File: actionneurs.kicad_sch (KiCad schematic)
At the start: 93 parts, among them J1 690367280876, J10 ESC_35_1_P, J11 690367280876, J12 ESC_35_2_S, J13 Alim Pompe, J14 690367280876, J16 690367280876, J17 690367280876, J18 690367280876, J19 Alim EV, J20 Alim EV, J21 Alim EV, J22 Alim EV, J23 Alim EV, J24 Alim EV, J25 Alim EV, J26 Alim EV, J27 Alim EV, J28 Alim EV, J29 Alim EV, J30 Alim EV, J6 ESC_35_1_P, J9 ESC_35_1_S, Q1 G2302, Q10 G2302, Q11 G2302, Q12 G2302, Q13 G2302, Q14 G2302, Q15 G2302, Q16 G2302, Q17 G2302, Q18 G2302, Q2 G2302, Q3 G2302, Q4 G2302, Q5 G2302

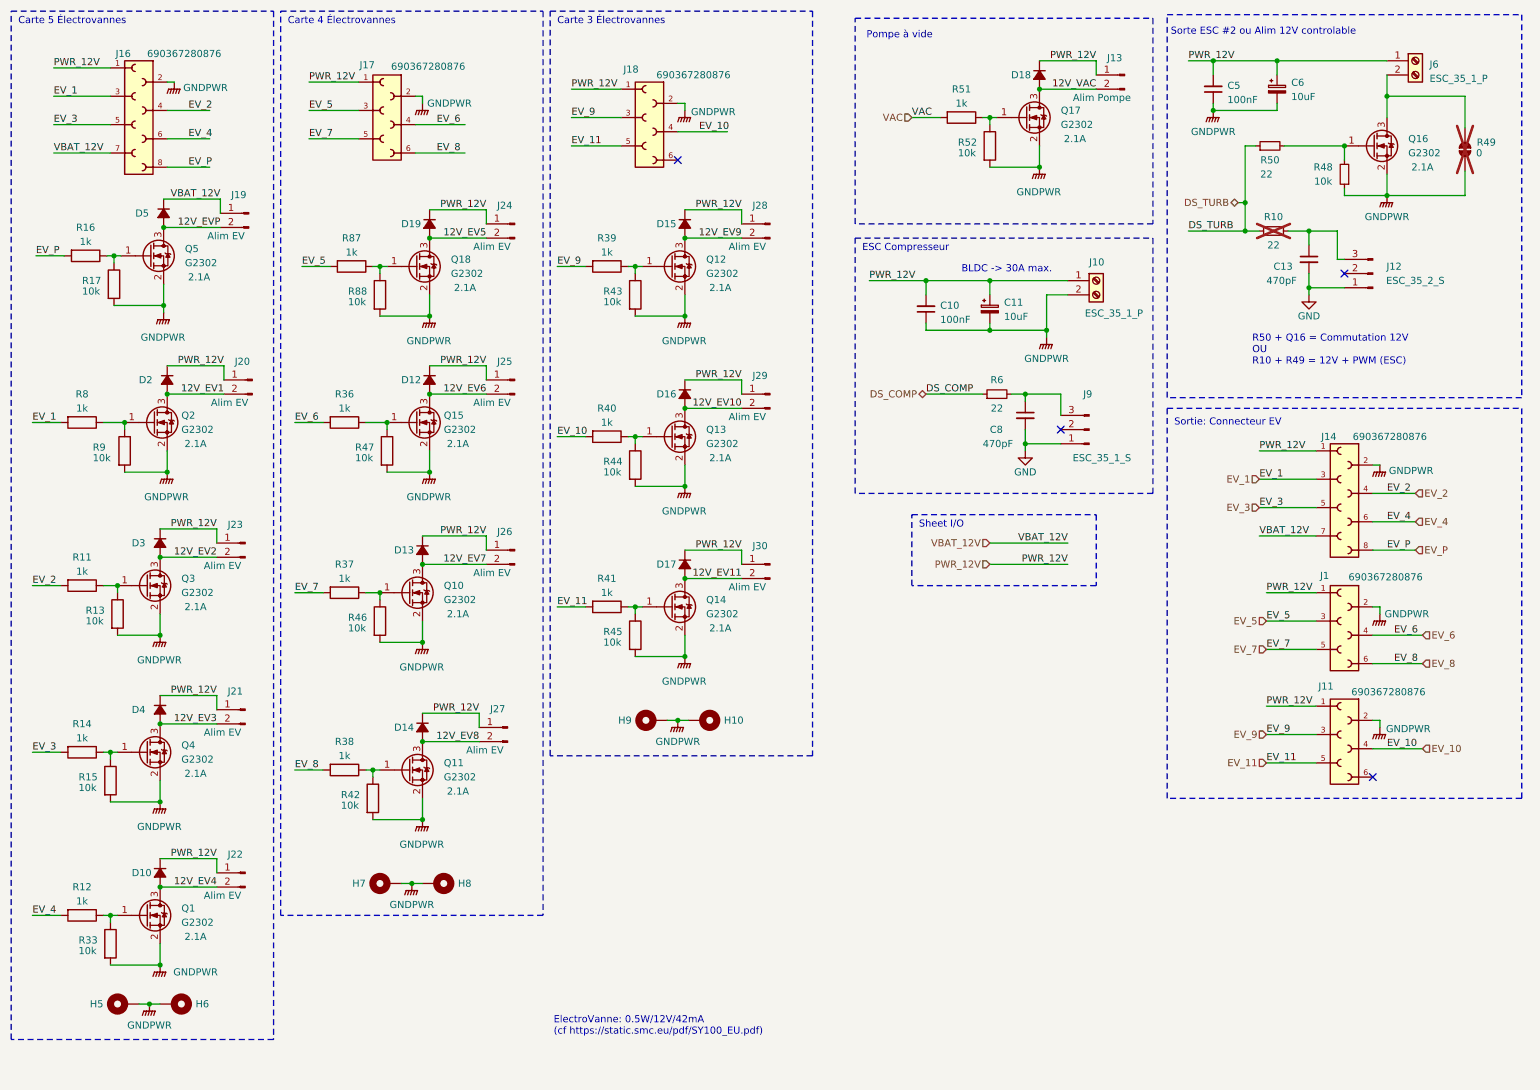
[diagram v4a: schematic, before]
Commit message: ajout regle routage JLCPCB, fin placement grossier et debut reassignation. ajout de led temoin, homogeinisation empreinte passif et remplacement 0ohm par empreintre jumper PCB 0402.
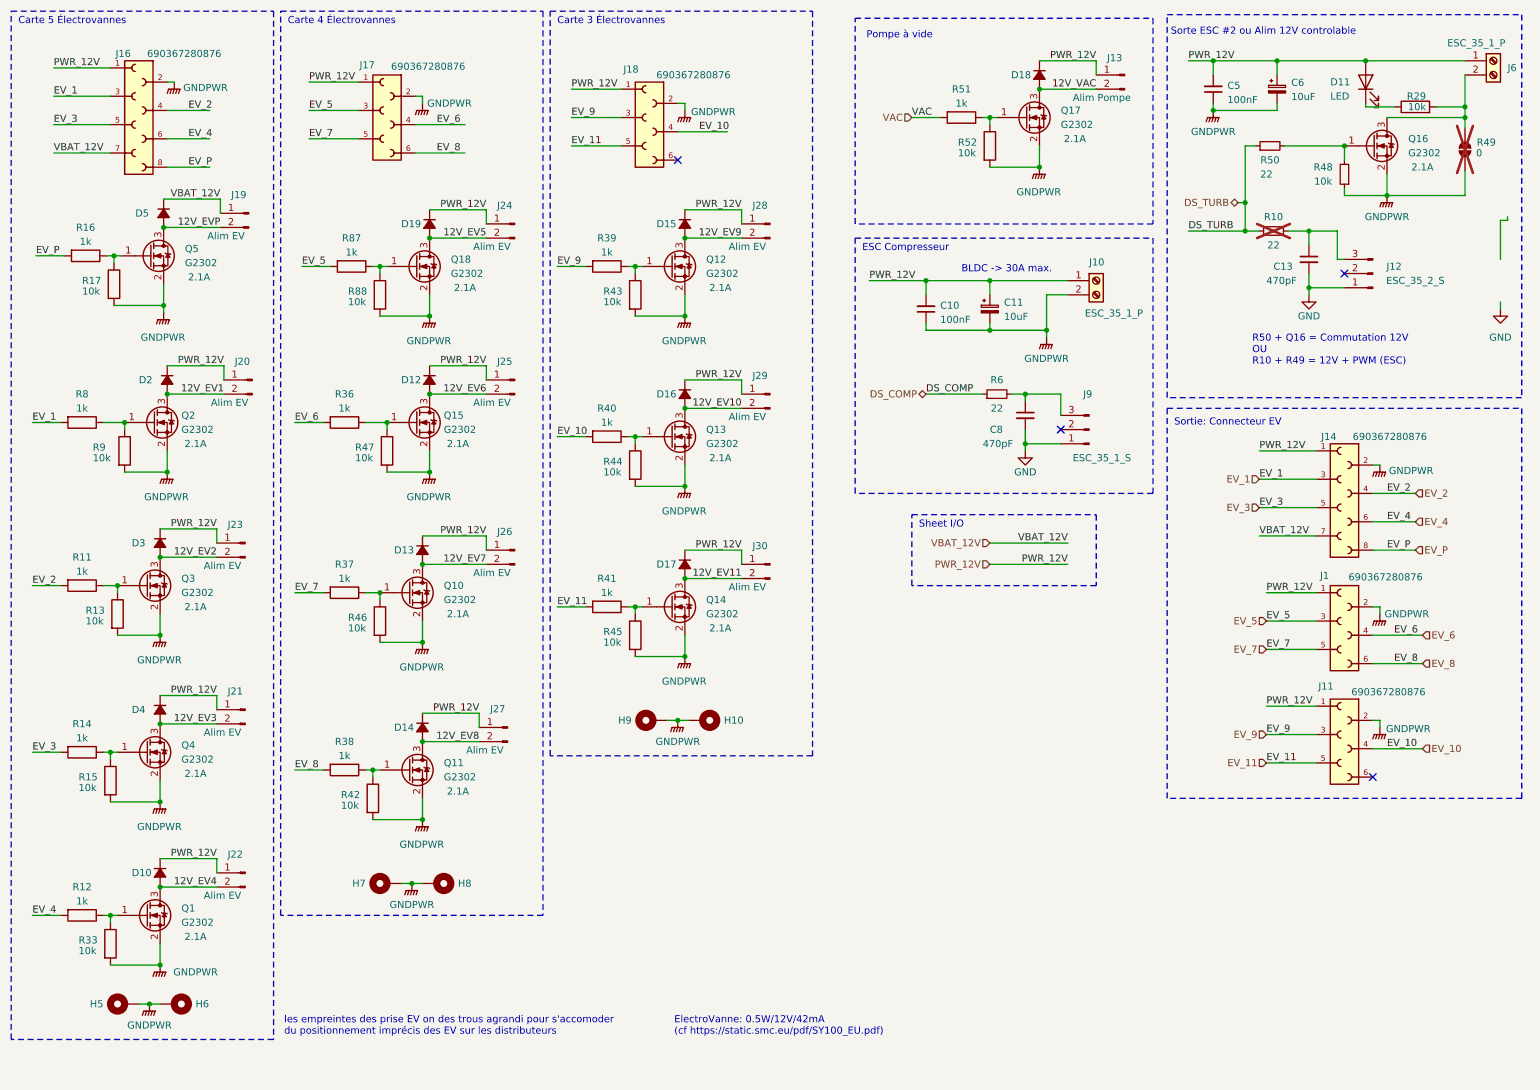
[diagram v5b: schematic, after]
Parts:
- added D11: LED, LED_SMD:LED_0603_1608Metric, symbol Device:LED
- added R29: 10k, Resistor_SMD:R_0603_1608Metric, symbol Device:R
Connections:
- net PWR_12V: now also D11.2 (A)
- net at J6.2 (Pin_2), Q16.3 (D), R49.1 (A): now also R29.2
- new net: D11.1 (K), R29.1
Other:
- note added: "les empreintes des prise EV on des trous agrandi pour s'accomoder du positionnement imprécis des EV sur les distributeurs"
- moved on the sheet: J6

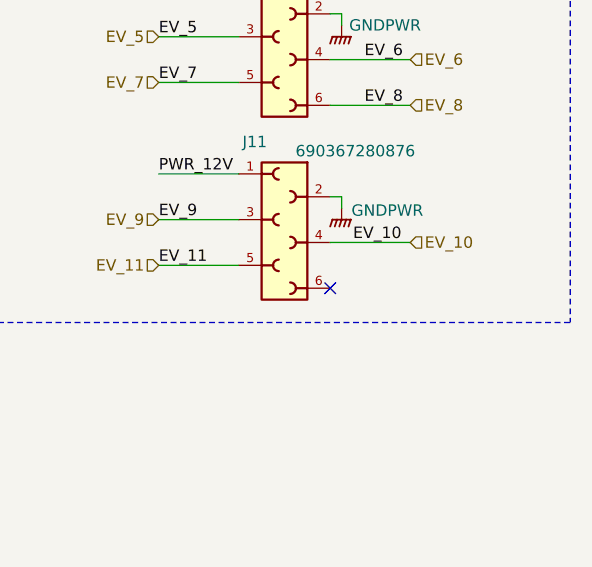
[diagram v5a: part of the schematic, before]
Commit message: fin du placement et reassignation des pins uC
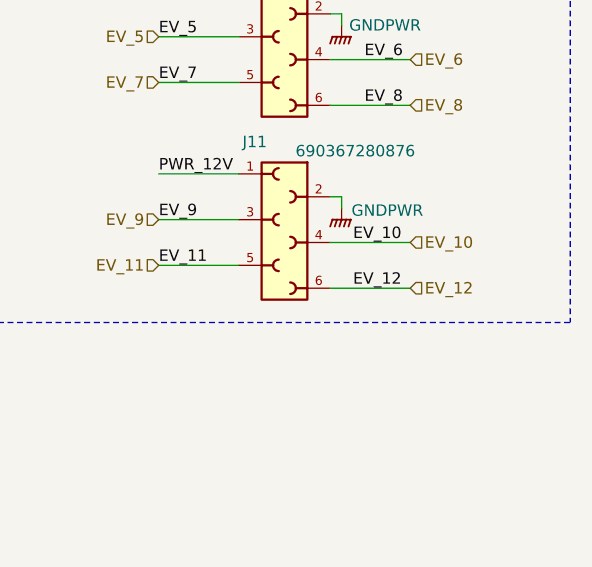
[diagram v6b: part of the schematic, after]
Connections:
- net EV_12: now reaches J11.6
- no-connect marks 4 -> 3
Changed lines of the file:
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@@
 	)
 	(no_connect
-		(at 256.54 149.86)
-	)
-	(no_connect
 		(at 132.08 39.37)
 	)
@@
 	(wire
 		(pts
+			(xy 256.54 149.86) (xy 265.43 149.86)
+		)
+		(stroke
+			(width 0)
+			(type default)
+		)
+	)
+	(wire
+		(pts
 			(xy 41.91 25.4) (xy 40.64 25.4)
 		)
@@
 		)
 	)
+	(label "EV_12"
+		(at 259.08 149.86 0)
+		(effects
+			(font
+				(size 1.27 1.27)
+			)
+			(justify left bottom)
+		)
+	)
 	(label "EV_1"
 		(at 236.22 96.52 0)
@@
 		)
 	)
+	(hierarchical_label "EV_12"
+		(shape input)
+		(at 265.43 149.86 0)
+		(effects
+			(font
+				(size 1.27 1.27)
+			)
+			(justify left)
+		)
+	)

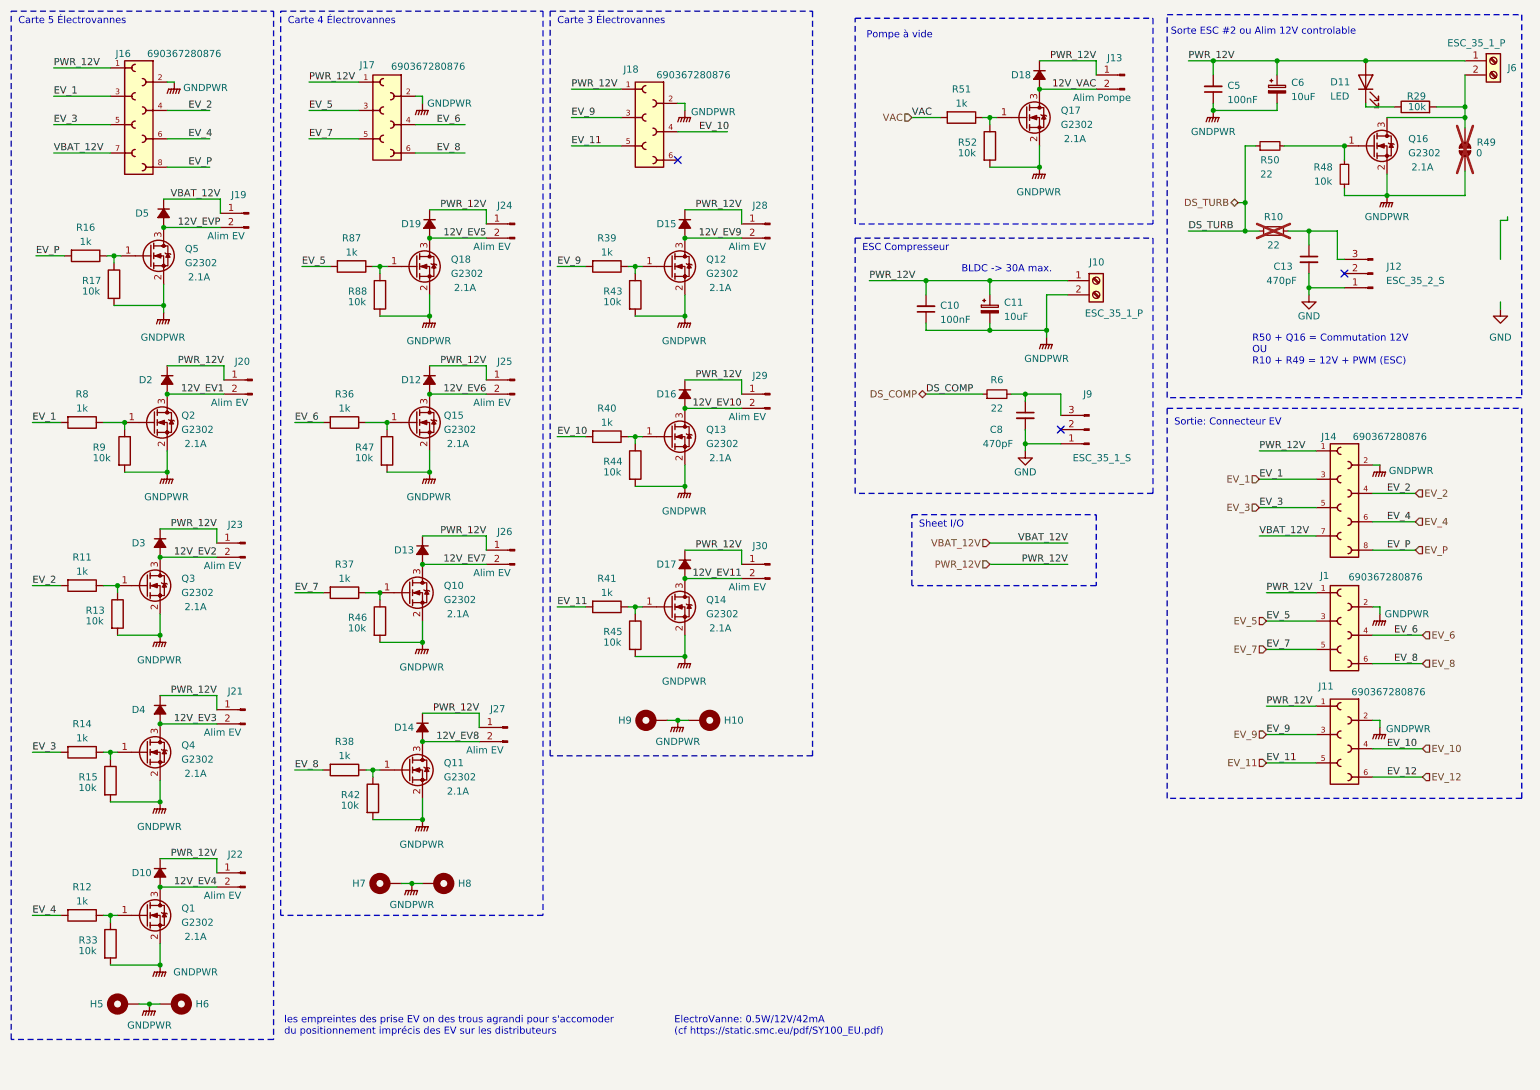
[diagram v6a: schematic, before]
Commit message: nettoyage dossier et assignation de ref JLCPCB
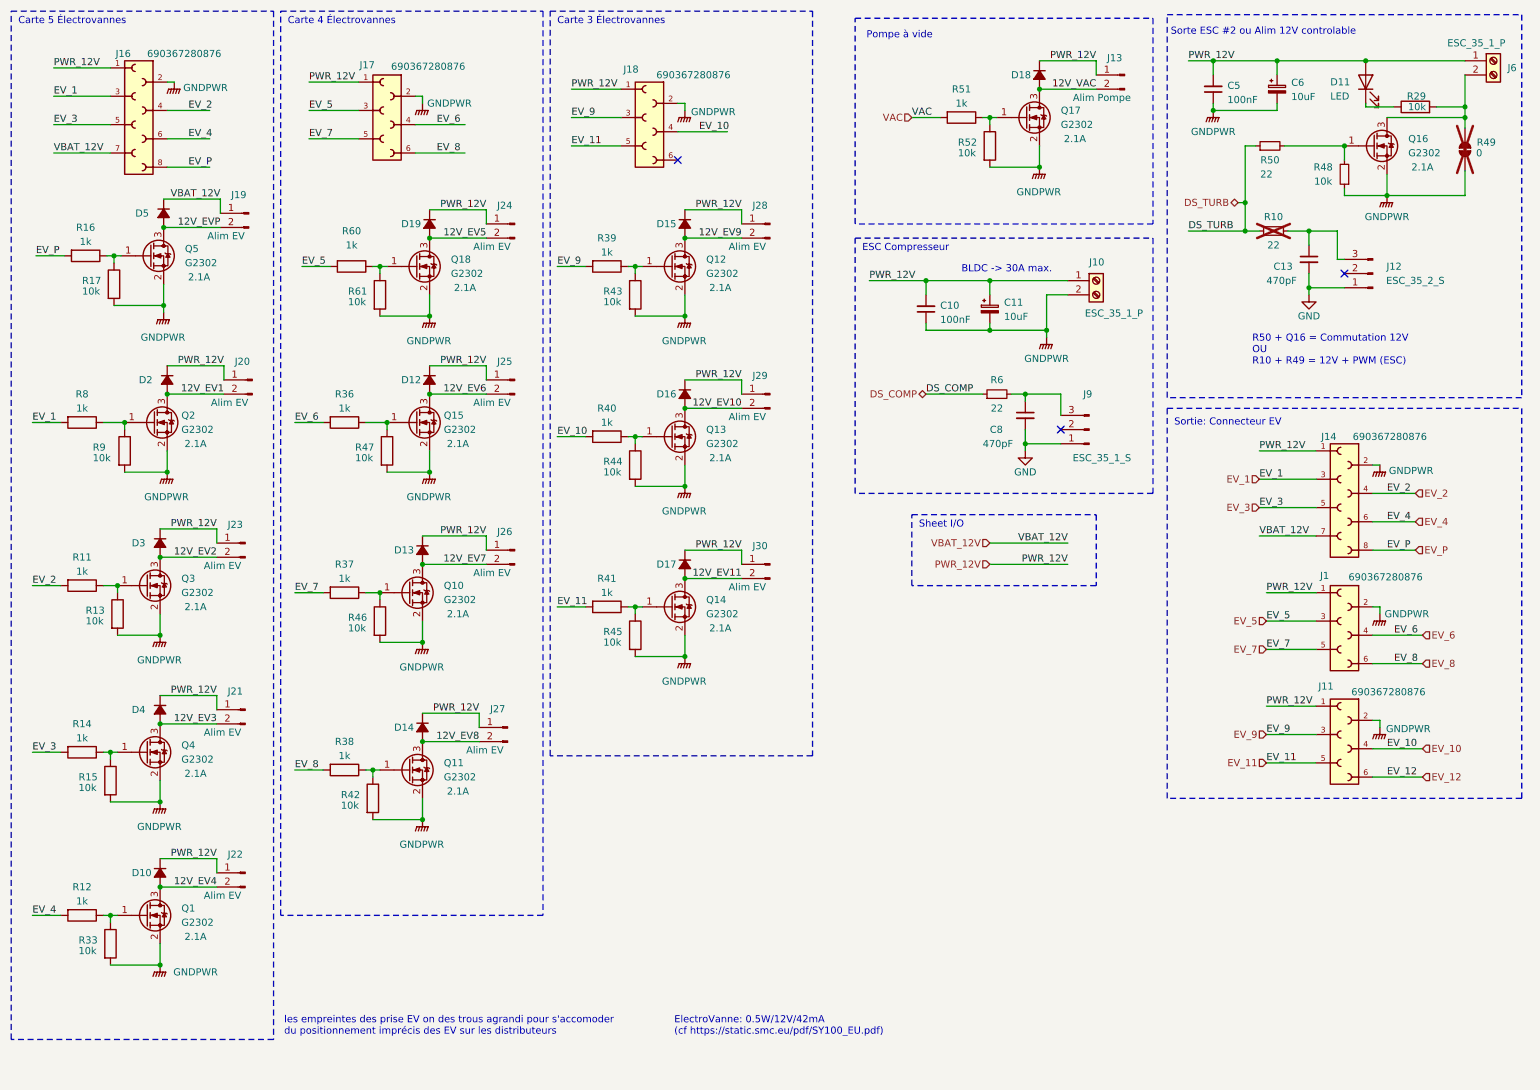
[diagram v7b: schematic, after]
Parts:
- removed H10, H5, H6, H7, H8, H9: MountingHole_Pad, MountingHole:MountingHole_3.2mm_M3_Pad, symbol Mechanical:MountingHole_Pad
- renumbered R87 to R60, R88 to R61
